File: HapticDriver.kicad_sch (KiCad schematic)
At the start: 14 parts, among them J14 USB_C_Receptacle_USB2.0, J3 BATT PWR, SW1 BOOT, SW2 EN, U1 ESP32-S3-WROOM-2, U11 REG1117-3.3, U3 74HCT595, U4 74HCT595, U5 74HCT595

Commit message: feat: pull OE and CLR shift reg pins to correct voltages
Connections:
- net +3V3: now also U3.10 (~{SRCLR}), U4.10 (~{SRCLR}), U5.10 (~{SRCLR})
- net GND: now also U3.13 (~{OE}), U4.13 (~{OE}), U5.13 (~{OE})
- no-connect marks 11 -> 10

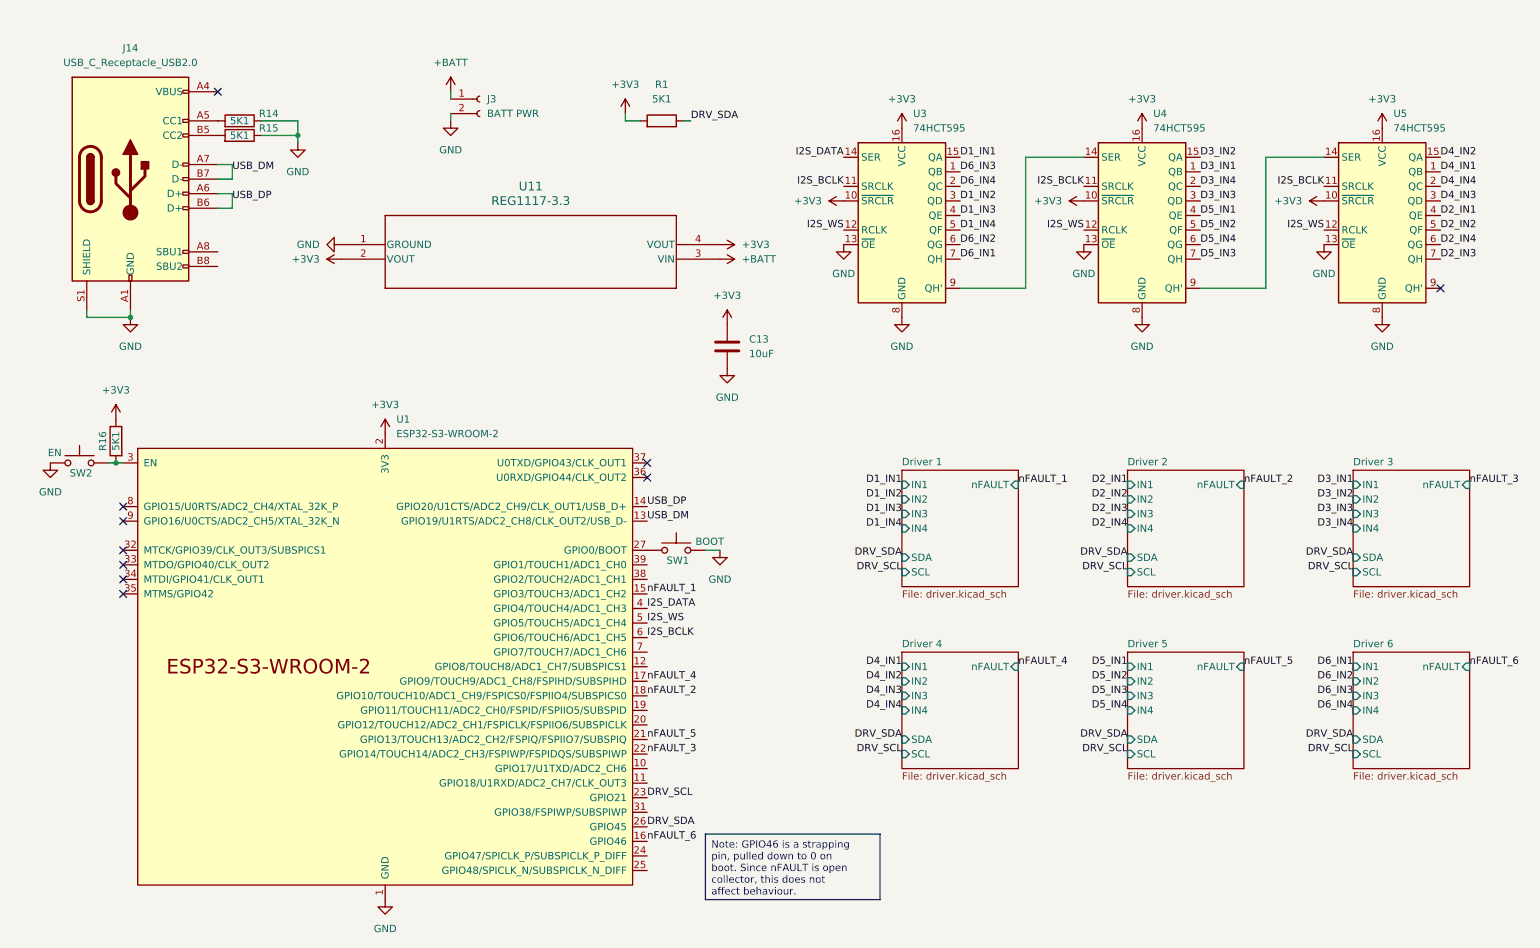
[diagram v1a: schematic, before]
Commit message: patch: mark unused pins
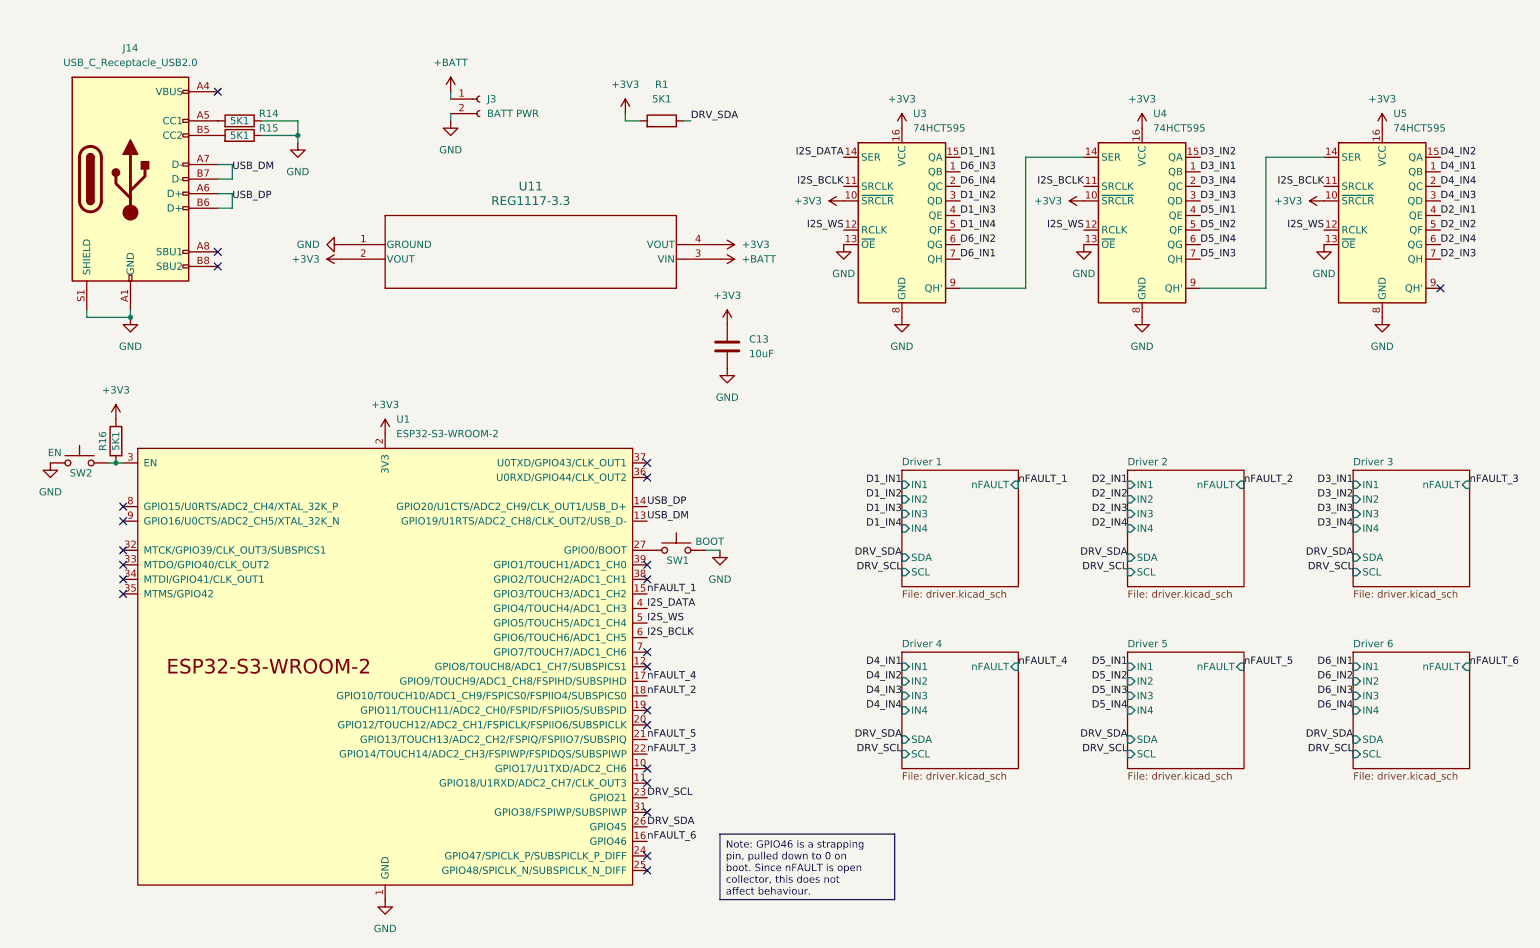
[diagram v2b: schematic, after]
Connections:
- no-connect marks 10 -> 23
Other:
- title: (none) -> HapticDriver
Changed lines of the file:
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@@
 	(generator_version "7.99")
 	(paper "A4")
+	(title_block
+		(title "HapticDriver")
+		(rev "v0.1")
+	)
 	(junction
 		(at 67.31 38.1)
@@
 	)
 	(no_connect
+		(at 128.27 113.03)
+	)
+	(no_connect
+		(at 128.27 130.81)
+	)
+	(no_connect
 		(at 128.27 95.25)
 	)
 	(no_connect
+		(at 128.27 115.57)
+	)
+	(no_connect
+		(at 53.34 58.42)
+	)
+	(no_connect
 		(at 36.83 105.41)
 	)
 	(no_connect
+		(at 128.27 148.59)
+	)
+	(no_connect
+		(at 128.27 163.83)
+	)
+	(no_connect
 		(at 36.83 113.03)
 	)
 	(no_connect
+		(at 53.34 60.96)
+	)
+	(no_connect
+		(at 128.27 166.37)
+	)
+	(no_connect
+		(at 128.27 138.43)
+	)
+	(no_connect
 		(at 53.34 30.48)
 	)
@@
 	)
 	(no_connect
+		(at 128.27 156.21)
+	)
+	(no_connect
+		(at 128.27 140.97)
+	)
+	(no_connect
 		(at 36.83 102.87)
+	)
+	(no_connect
+		(at 128.27 151.13)
+	)
+	(no_connect
+		(at 128.27 128.27)
 	)
 	(no_connect
@@
 	(text_box "Note: GPIO46 is a strapping pin, pulled down to 0 on boot. Since nFAULT is open collector, this does not affect behaviour."
 		(exclude_from_sim no)
-		(at 138.43 160.02 0)
+		(at 140.97 160.02 0)
 		(size 30.48 11.43)
 		(stroke

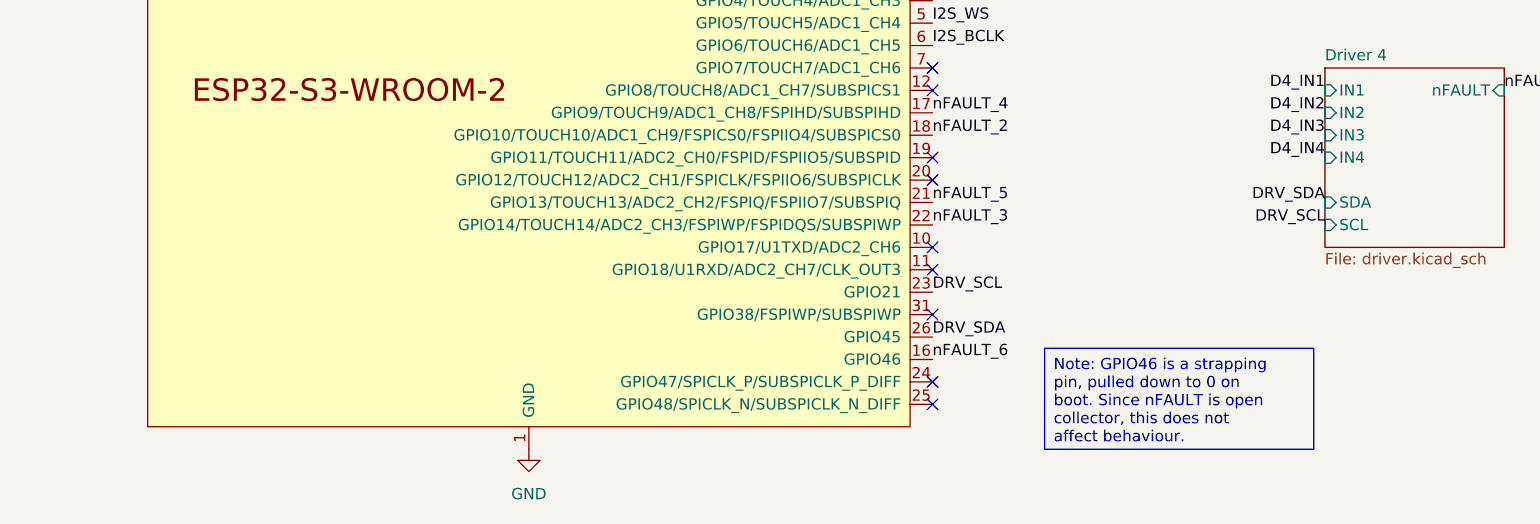
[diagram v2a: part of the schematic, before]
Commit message: fix: avoid SDA on strapping pin GPIO45
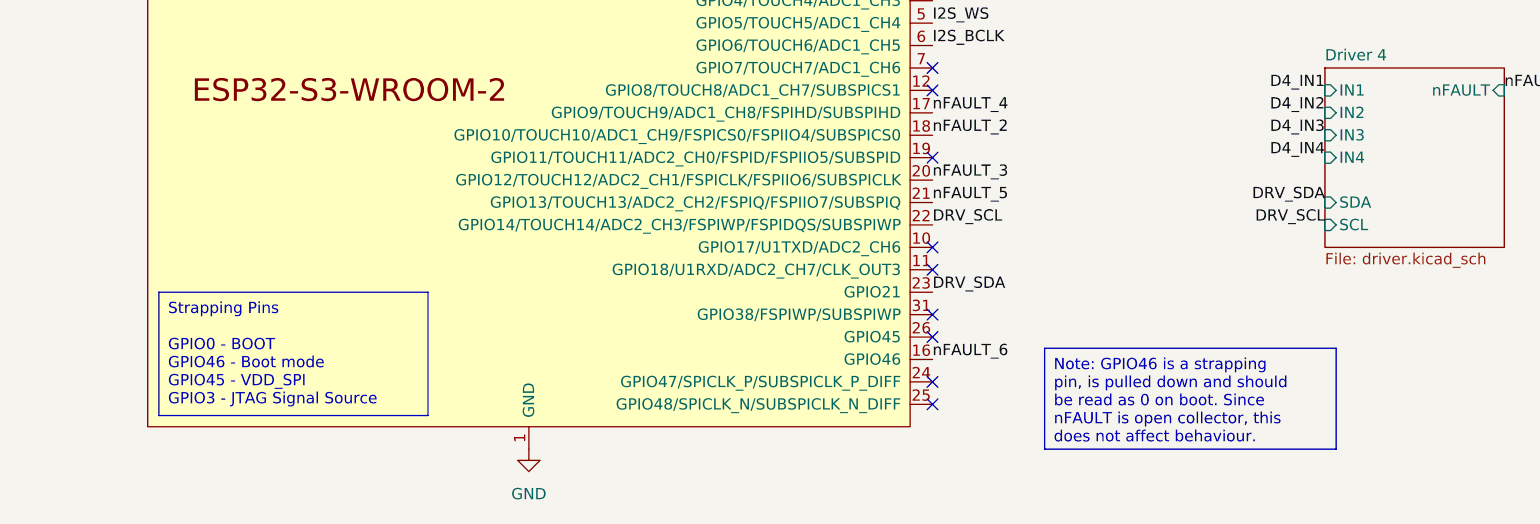
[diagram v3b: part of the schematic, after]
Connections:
- net DRV_SCL: now also U1.22 (GPIO14/TOUCH14/ADC2_CH3/FSPIWP/FSPIDQS/SUBSPIWP); no longer U1.23 (GPIO21)
- net DRV_SDA: now also U1.23 (GPIO21); no longer U1.26 (GPIO45)
- net nFAULT_3: now also U1.20 (GPIO12/TOUCH12/ADC2_CH1/FSPICLK/FSPIIO6/SUBSPICLK); no longer U1.22 (GPIO14/TOUCH14/ADC2_CH3/FSPIWP/FSPIDQS/SUBSPIWP)

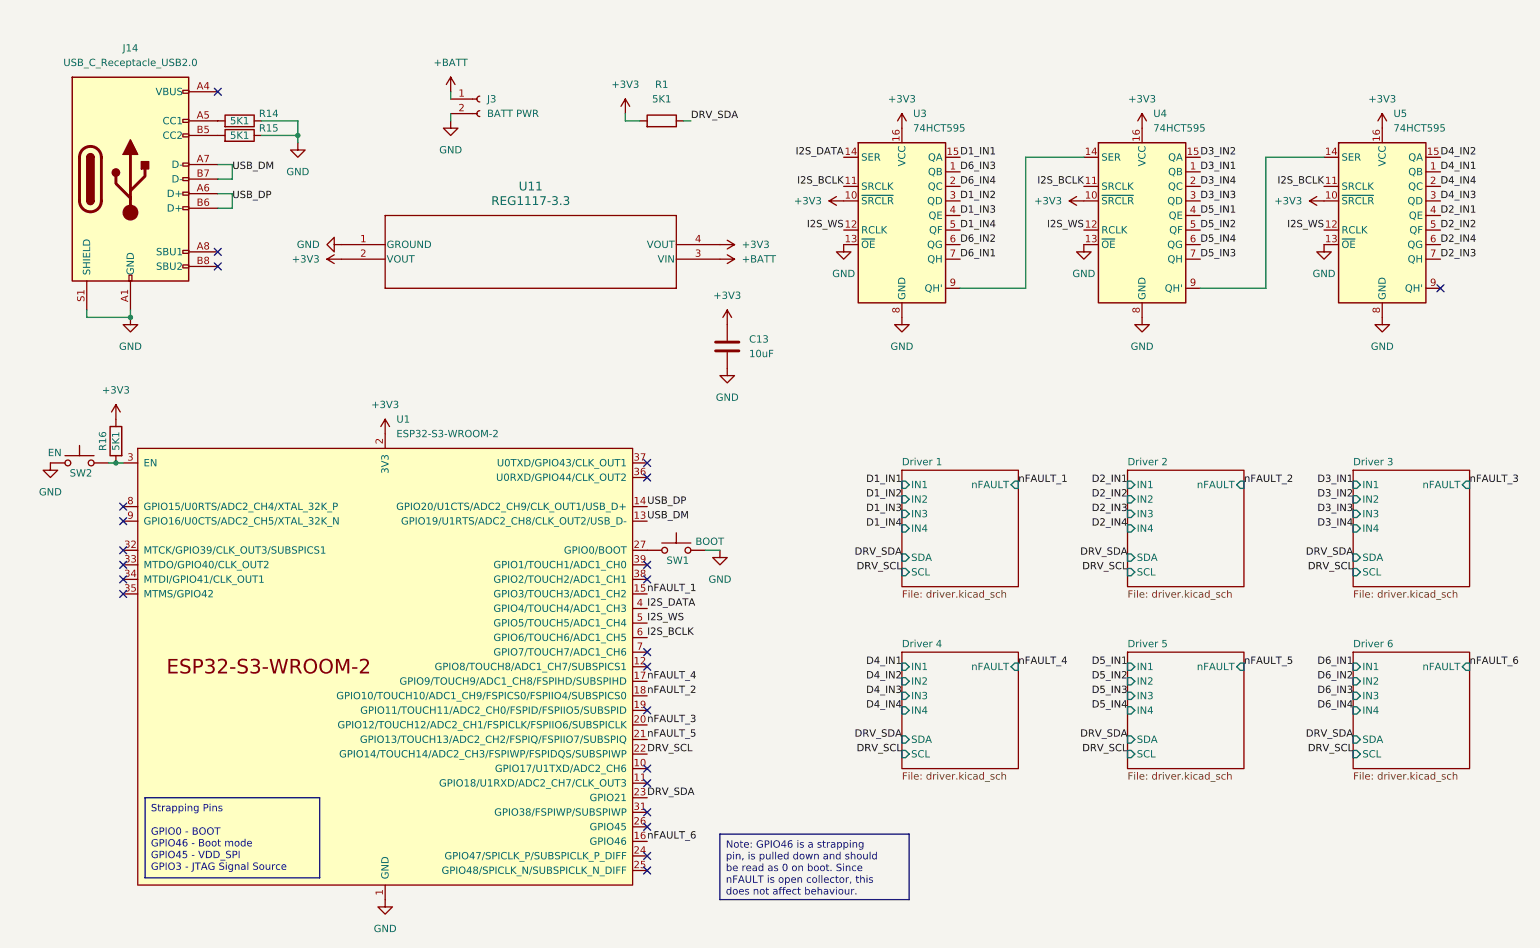
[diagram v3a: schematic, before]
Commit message: fix: delay rising of EN with cap, as per devkit design
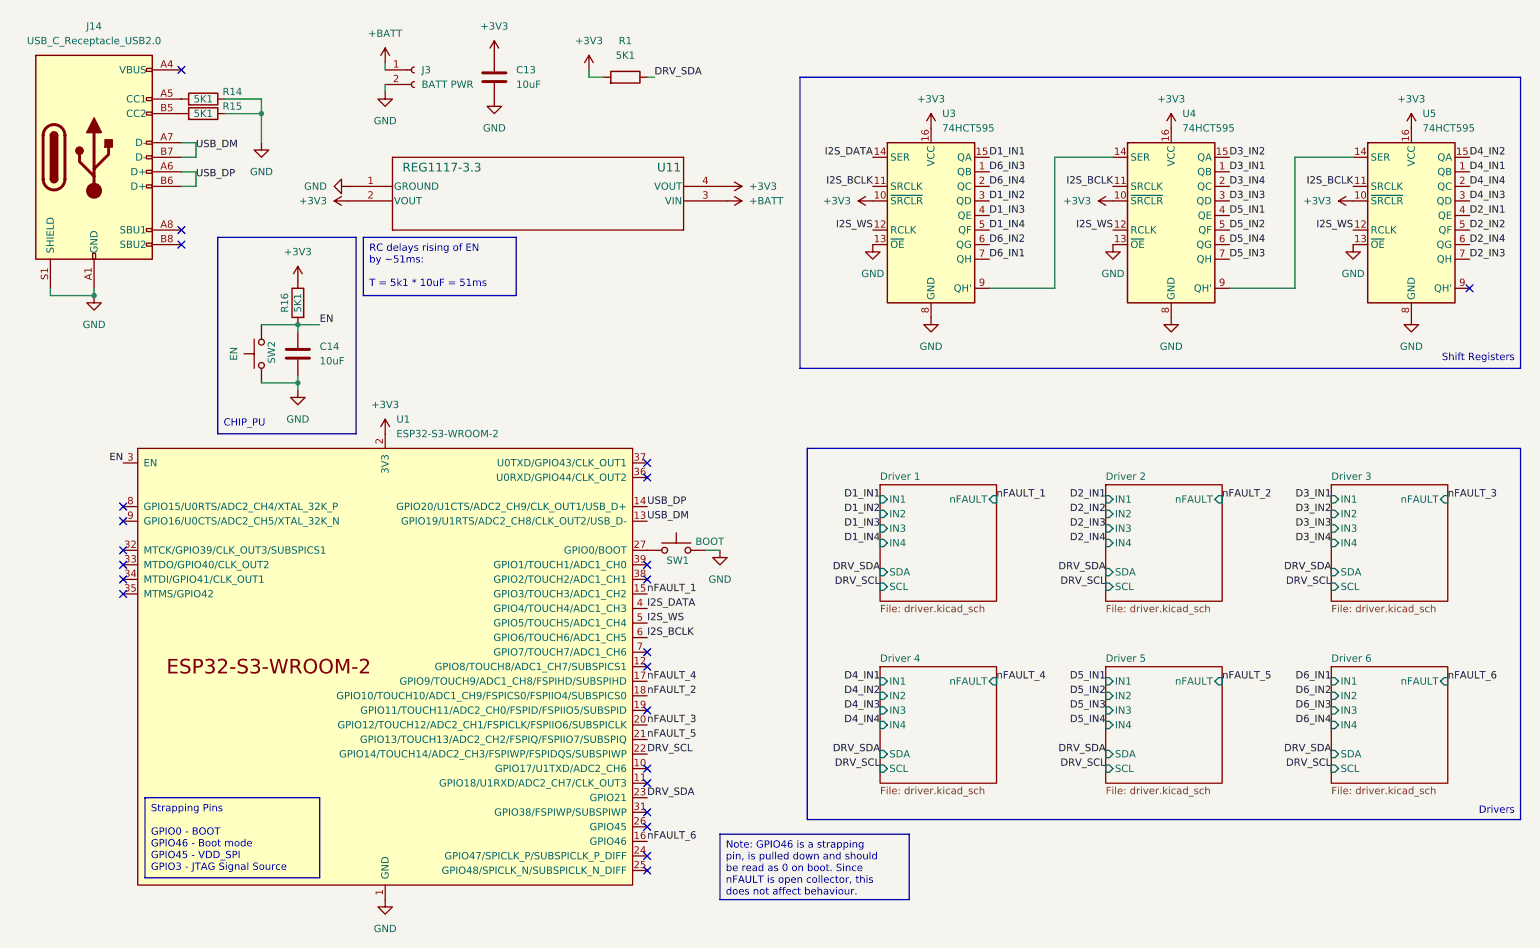
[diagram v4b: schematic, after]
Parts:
- added C14: 10uF, Capacitor_SMD:C_1206_3216Metric_Pad1.33x1.80mm_HandSolder, symbol Device:C
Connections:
- net GND: now also C14.2
- net EN: now reaches R16.2, SW2.2, U1.3 (EN)
- net EN: now also C14.1
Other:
- note added: "CHIP_PU"
- note added: "Drivers"
- note added: "Shift Registers"
- moved on the sheet: C13, J14, J3, R1, R14, R15, R16, SW2, U11, U3, U4, U5

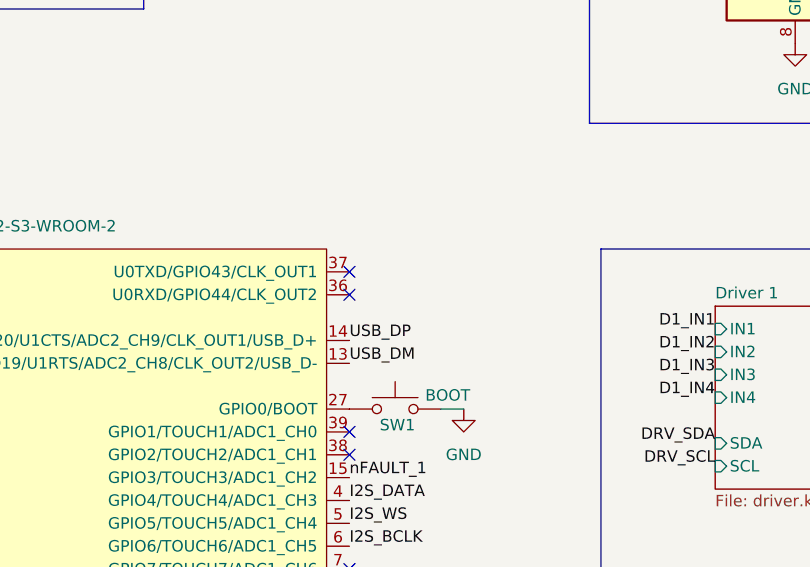
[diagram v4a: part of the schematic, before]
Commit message: patch: improve silkscreen, add testpoints, optimise some traces
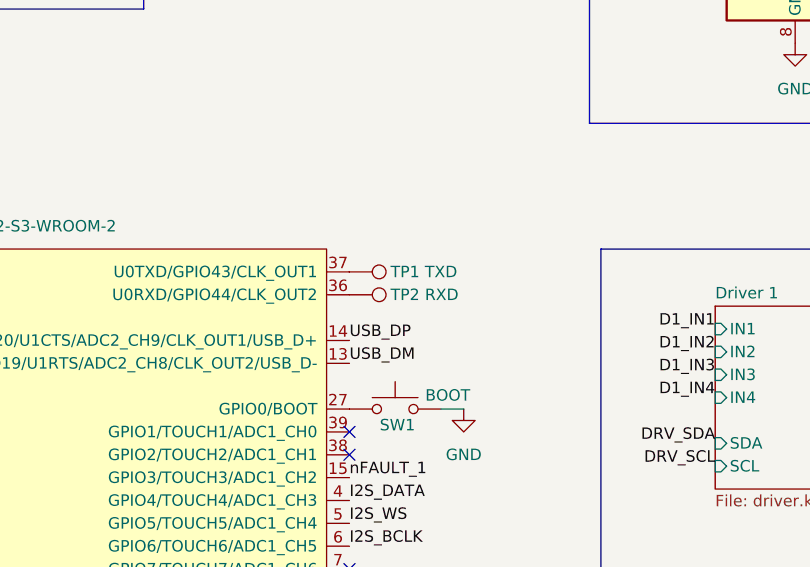
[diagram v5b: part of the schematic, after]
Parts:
- added TP1: TXD, TestPoint:TestPoint_Pad_1.5x1.5mm, symbol Connector:TestPoint
- added TP2: RXD, TestPoint:TestPoint_Pad_1.5x1.5mm, symbol Connector:TestPoint
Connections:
- net at U1.36 (U0RXD/GPIO44/CLK_OUT2): now also TP2.1
- net at U1.37 (U0TXD/GPIO43/CLK_OUT1): now also TP1.1
- no-connect marks 23 -> 21
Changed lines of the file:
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@@
 	)
 	(no_connect
-		(at 128.27 97.79)
-	)
-	(no_connect
 		(at 128.27 113.03)
 	)
@@
 	)
 	(no_connect
-		(at 128.27 95.25)
-	)
-	(no_connect
 		(at 128.27 115.57)
 	)
@@
 	)
 	(symbol
+		(lib_id "Connector:TestPoint")
+		(at 128.27 97.79 270)
+		(unit 1)
+		(exclude_from_sim no)
+		(in_bom yes)
+		(on_board yes)
+		(dnp no)
+		(property "Reference" "TP2"
+			(at 132.842 97.79 90)
+			(effects
+				(font
+					(size 1.27 1.27)
+				)
+				(justify left)
+			)
+		)
+		(property "Value" "RXD"
+			(at 136.652 97.79 90)
+			(effects
+				(font
+					(size 1.27 1.27)
+				)
+				(justify left)
+			)
+		)
+		(property "Footprint" "TestPoint:TestPoint_Pad_1.5x1.5mm"
+			(at 128.27 102.87 0)
+			(effects
+				(font
+					(size 1.27 1.27)
+				)
+				(hide yes)
+			)
+		)
+		(property "Datasheet" "~"
+			(at 128.27 102.87 0)
+			(effects
+				(font
+					(size 1.27 1.27)
+				)
+				(hide yes)
+			)
+		)
+		(property "Description" "test point"
+			(at 128.27 97.79 0)
+			(effects
+				(font
+					(size 1.27 1.27)
+				)
+				(hide yes)
+			)
+		)
+		(pin "1"
+		)
+		(instances
+			(project "HapticDriver"
+				(path "/89c84321-602a-4eb8-8dad-33289e154cd9"
+					(reference "TP2")
+					(unit 1)
+				)
+			)
+		)
+	)
+	(symbol
 		(lib_id "power:GND")
 		(at 177.8 69.85 0)
@@
 					(unit 1)
 				)
+			)
+		)
+	)
+	(symbol
+		(lib_id "Connector:TestPoint")
+		(at 128.27 95.25 270)
+		(unit 1)
+		(exclude_from_sim no)
+		(in_bom yes)
+		(on_board yes)
+		(dnp no)
+		(property "Reference" "TP1"
+			(at 132.842 95.25 90)
+			(effects
+				(font
+					(size 1.27 1.27)
+				)
+				(justify left)
+			)
+		)
+		(property "Value" "TXD"
+			(at 136.652 95.25 90)
+			(effects
+				(font
+					(size 1.27 1.27)
+				)
+				(justify left)
+			)
+		)
+		(property "Footprint" "TestPoint:TestPoint_Pad_1.5x1.5mm"
+			(at 128.27 100.33 0)
+			(effects
+				(font
+					(size 1.27 1.27)
+				)
+				(hide yes)
+			)
+		)
+		(property "Datasheet" "~"
+			(at 128.27 100.33 0)
+			(effects
+				(font
+					(size 1.27 1.27)
+				)
+				(hide yes)
+			)
+		)
+		(property "Description" "test point"
+			(at 128.27 95.25 0)
+			(effects
+				(font
+					(size 1.27 1.27)
+				)
+				(hide yes)
+			)
+		)
+		(pin "1"
+		)
+		(instances
+			(project "HapticDriver"
+				(path "/89c84321-602a-4eb8-8dad-33289e154cd9"
+					(reference "TP1")
+					(unit 1)
+				)

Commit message: patch: final touch-ups, v0.1 fabrication
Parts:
- added C15: 10uF, Capacitor_SMD:C_1206_3216Metric_Pad1.33x1.80mm_HandSolder, symbol Device:C
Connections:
- net +BATT: now also C15.1
- net GND: now also C15.2
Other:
- moved on the sheet: C13, R1, U11
